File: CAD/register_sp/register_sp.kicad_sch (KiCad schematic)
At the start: 35 parts, among them J1 Conn_01x18_Pin, J2 Conn_01x18_Pin, U1 74HC377, U2 74HC245, U3 74HC283, U4 74HC283, U5 74HC157, U6 74HC157, U7 74HC02, U8 74HC08

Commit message: add SP layout without routing
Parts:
- added D10: OUT, LED_SMD:LED_0805_2012Metric, symbol Device:LED
- added D11: INC, LED_SMD:LED_0805_2012Metric, symbol Device:LED
- added D12: DEC, LED_SMD:LED_0805_2012Metric, symbol Device:LED
- added D9: LOAD, LED_SMD:LED_0805_2012Metric, symbol Device:LED
- added FID1, FID2: Fiducial, Fiducial:Fiducial_0.5mm_Mask1mm, symbol Mechanical:Fiducial
- added H1, H2: MountingHole_Pad, MountingHole:MountingHole_2.5mm_Pad_Via, symbol Mechanical:MountingHole_Pad
- added H3, H4, H5, H6: ToolingHole, MountingHole:ToolingHole_1.152mm, symbol Mechanical:MountingHole
- added R10, R11, R12, R9: 1k, Resistor_SMD:R_0805_2012Metric, symbol Device:R
- added R13: 10k, Resistor_SMD:R_0805_2012Metric, symbol Device:R
- added TP1, TP2, TP3, TP4: TestPoint, TestPoint:TestPoint_THTPad_D1.0mm_Drill0.5mm, symbol Connector:TestPoint
- added unit 1 of U7
- added unit 4 of U7
- added unit 5 of U7
- added unit 3 of U7
- added unit 1 of U8
- added unit 2 of U8
- added unit 5 of U8
- added unit 4 of U8
- C1: renamed from C9; footprint (none) -> Capacitor_SMD:C_0805_2012Metric
- C2, C3, C4, C5, C6, C7, C8: footprint (none) -> Capacitor_SMD:C_0805_2012Metric
- C9: renamed from C1; footprint (none) -> Capacitor_SMD:C_0805_2012Metric
- J1: footprint (none) -> Connector_PinHeader_2.54mm:PinHeader_2x09_P2.54mm_Horizontal
- J2: footprint (none) -> Connector_PinSocket_2.54mm:PinSocket_2x09_P2.54mm_Horizontal
- U1: footprint (none) -> 8-bit_computer:SO-20_5.3x12.6mm_P1.27mm; Details (none) -> https://www.lcsc.com/product-detail/C7647.html; LCSC (none) -> C7647
- U2: footprint (none) -> Package_SO:SOIC-20W_7.5x12.8mm_P1.27mm; symbol 74xx:74HC245 -> 8bit_computer:74HC245; Details (none) -> https://jlcpcb.com/partdetail/Nexperia-74HC245D653/C5625; LCSC (none) -> C5625
- U3, U4: footprint (none) -> Package_SO:SO-16_3.9x9.9mm_P1.27mm; Details (none) -> https://www.lcsc.com/product-detail/C24833609.html; LCSC (none) -> C24833609
- U5, U6: footprint (none) -> Package_SO:SO-16_3.9x9.9mm_P1.27mm; Details (none) -> https://www.lcsc.com/product-detail/C6823.html; LCSC (none) -> C6823
- U7: footprint (none) -> Package_SO:SO-14_3.9x8.65mm_P1.27mm; symbol 74xx:74HC02 -> 8bit_computer:74HC02; Details (none) -> https://www.lcsc.com/product-detail/C350559.html; LCSC (none) -> C350559
- U8: footprint (none) -> Package_SO:SO-14_3.9x8.65mm_P1.27mm; Details (none) -> https://jlcpcb.com/partdetail/Nexperia-74HC08D653/C5593; LCSC (none) -> C5593
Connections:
- net +5V: now also R10.1, R13.2, R9.1, TP1.1, U7.14 (VCC), U8.14 (VCC); no longer U2.1 (A->B), U7.14 (VCC), U8.14 (VCC)
- net GND: now also U2.1 (A->B), D11.1 (K), D12.1 (K), H1.1, H2.1, TP2.1, TP4.1, U7.11, U7.12, U7.7 (GND), U7.8, U7.9, U8.12, U8.13, U8.7 (GND); no longer U7.11, U7.12, U7.7 (GND), U7.8, U7.9, U8.12, U8.13, U8.7 (GND)
- net clk: now also TP3.1
- net dbus0: now also U2.2 (A0); no longer U2.18 (B0)
- net dbus1: now also U2.3 (A1); no longer U2.17 (B1)
- net dbus2: now also U2.4 (A2); no longer U2.16 (B2)
- net dbus3: now also U2.5 (A3); no longer U2.15 (B3)
- net dbus4: now also U2.6 (A4); no longer U2.14 (B4)
- net dbus5: now also U2.7 (A5); no longer U2.13 (B5)
- net dbus6: now also U2.8 (A6); no longer U2.12 (B6)
- net dbus7: now also U2.9 (A7); no longer U2.11 (B7)
- net dec: now also R12.1, U8.5; no longer U8.5
- net dec_out: now also U8.6; no longer U8.6
- net inc: now also R11.1, U8.1; no longer U8.1
- net inc_out: now also U8.3; no longer U8.3
- net q0: now also U2.18 (B0); no longer U2.2 (A0)
- net q1: now also U2.17 (B1); no longer U2.3 (A1)
- net q2: now also U2.16 (B2); no longer U2.4 (A2)
- net q3: now also U2.15 (B3); no longer U2.5 (A3)
- net q4: now also U2.14 (B4); no longer U2.6 (A4)
- net q5: now also U2.13 (B5); no longer U2.7 (A5)
- net q6: now also U2.12 (B6); no longer U2.8 (A6)
- net q7: now also U2.11 (B7); no longer U2.9 (A7)
- net carry: now reaches U3.9 (C4), U4.7 (C0)
- net ~{reg_load}: now reaches U1.1 (~{E}), U8.8
- net inv2: now reaches U7.4, U8.9
- net reg1_in renamed ~{reg1_in}
- net ~{reg1_in}: now also D9.1 (K)
- net reg1_out renamed ~{reg1_out}
- net ~{reg1_out}: now also D10.1 (K), R13.1
- net reg2_in renamed ~{reg2_in}
- net reg2_out renamed ~{reg2_out}
- net rst renamed ~{rst}
- new net: D10.2 (A), R10.2
- new net: D11.2 (A), R11.2
- new net: D9.2 (A), R9.2
- new net: D12.2 (A), R12.2
- new net carry_out: U4.9 (C4), U7.2, U7.3, U8.2
- new net inv1: U7.1, U8.4
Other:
- note added: "TESTPOINTS"
- title: (none) -> ${TITLE}
- moved on the sheet: C1, C2, C3, C4, C5, C6, C7, C8, C9, D1, D2, D3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

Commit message: add SP PCB
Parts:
- added R14, R15: 10k, Resistor_SMD:R_0805_2012Metric, symbol Device:R
- C1, C2, C3, C4, C5, C6, C7, C8: LCSC (none) -> C28233
- C9: LCSC (none) -> C15850
- D1, D2, D3, D4, D5, D6, D7, D8: LCSC (none) -> C84256
- D10: LCSC (none) -> C2296
- D9: LCSC (none) -> C2297
- J1: LCSC (none) -> C18905907
- J2: LCSC (none) -> C2897429
- R1, R10, R11, R12, R2, R3, R4, R5, R6, R7, R8, R9: LCSC (none) -> C17513
- R13: LCSC (none) -> C17414
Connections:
- net +5V: now also J2.3 (Pin_3), J2.4 (Pin_4)
- net GND: now also R14.1, R15.1
- net dec: now also R15.2
- net inc: now also R14.2
- no-connect marks 5 -> 3
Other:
- moved on the sheet: C1, C2, C3, C4, C5, C6, C7, C8, D10, D11, D12, D9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

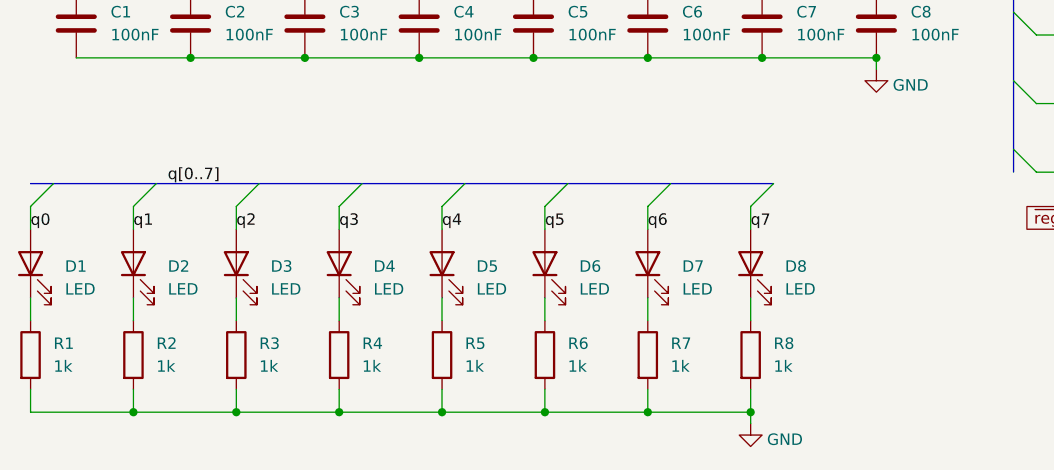
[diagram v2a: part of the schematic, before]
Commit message: SP layout improvements
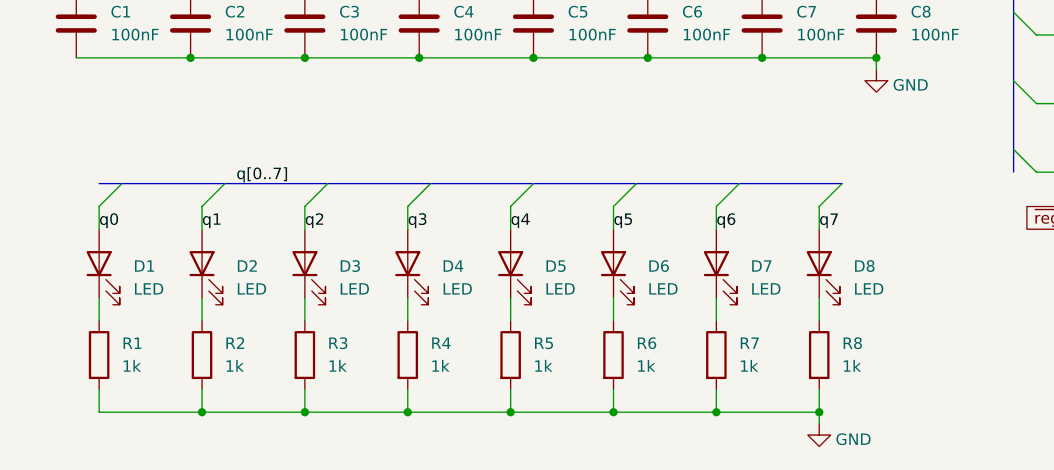
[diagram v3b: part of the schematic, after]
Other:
- moved on the sheet: D1, D2, D3, D4, D5, D6, D7, D8, R1, R2, R3, R4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

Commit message: update SP - change board order
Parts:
- J1: value Conn_01x18_Pin -> Conn_01x20_Pin; footprint Connector_PinHeader_2.54mm:PinHeader_2x09_P2.54mm_Horizontal -> Connector_PinHeader_2.54mm:PinHeader_2x10_P2.54mm_Horizontal; symbol Connector:Conn_01x18_Pin -> Connector:Conn_01x20_Pin
- J2: value Conn_01x18_Pin -> Conn_01x20_Pin; footprint Connector_PinSocket_2.54mm:PinSocket_2x09_P2.54mm_Horizontal -> Connector_PinSocket_2.54mm:PinSocket_2x10_P2.54mm_Horizontal; symbol Connector:Conn_01x18_Pin -> Connector:Conn_01x20_Pin
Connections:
- net dec_out: now also J1.1 (Pin_1); no longer J2.1 (Pin_1)
- net inc_out: now also J1.19 (Pin_19); no longer J2.2 (Pin_2)
- net dec renamed dec_in
- net dec_in: now also J2.1 (Pin_1); no longer J1.1 (Pin_1)
- net inc renamed inc_in
- net inc_in: now also J2.19 (Pin_19); no longer J1.2 (Pin_2)
- new net dec_lsb: J1.2 (Pin_2), J2.2 (Pin_2)
- new net inc_lsb: J1.20 (Pin_20), J2.20 (Pin_20)
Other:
- moved on the sheet: C9
